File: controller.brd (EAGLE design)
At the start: 61 x 38.1 mm, 26 parts, among them U1 ATMEGA328P_PDIP, Y1 16MHz

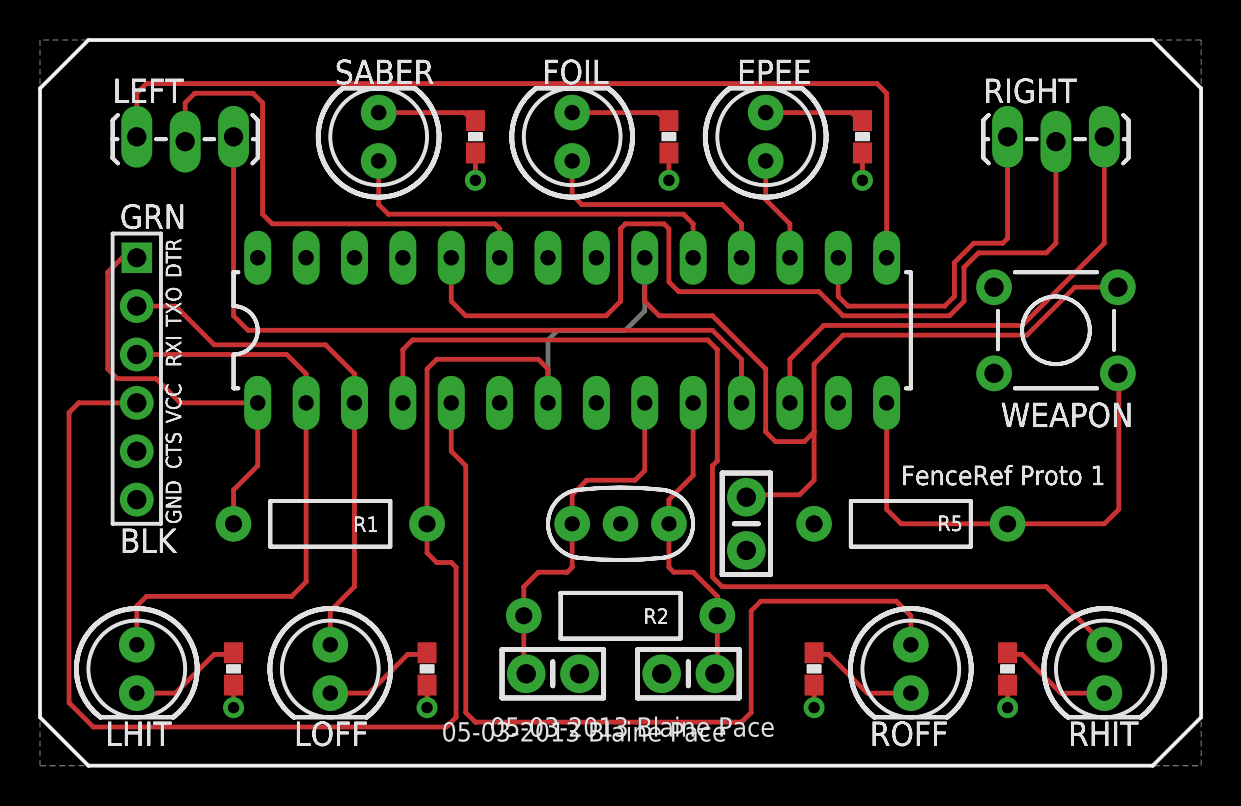
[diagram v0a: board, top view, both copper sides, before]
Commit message: Replaced resonator with crystal and updated CAM job
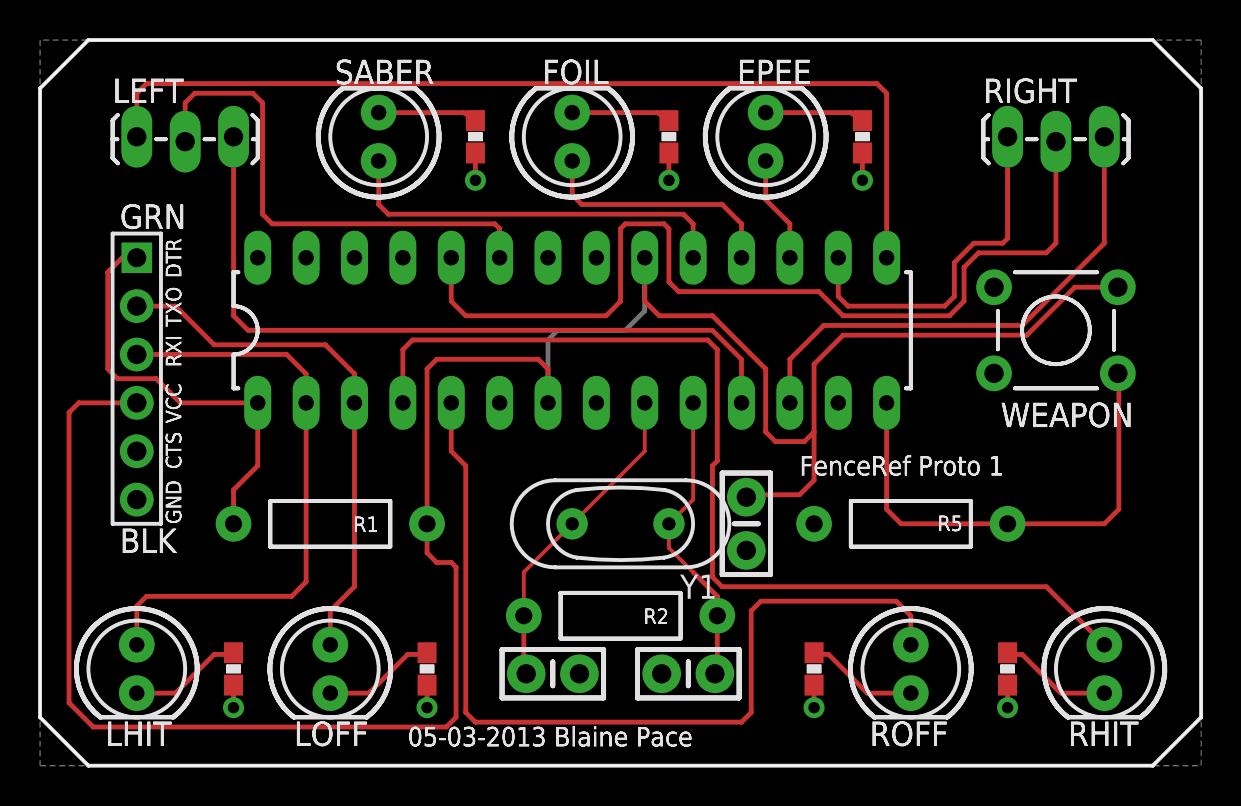
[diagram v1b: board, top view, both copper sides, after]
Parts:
- Y1: value 16MHz -> (none); device SparkFun-FreqCtrl:RESONATOR-PTH -> SparkFun-FreqCtrl:HC49US
- turned Y1 to 180 degrees
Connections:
- net GND: no longer Y1.2
- net XTAL1: now also Y1.2; no longer Y1.1
- net XTAL2: now also Y1.1; no longer Y1.3
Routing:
- net XTAL1: track 19.3 -> 16.9 mm
- net XTAL2: track 16.4 -> 15.9 mm
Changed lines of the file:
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@@
 <wire x1="2.54" y1="0" x2="0" y2="2.54" width="0" layer="20"/>
 <wire x1="0" y1="2.54" x2="0" y2="35.56" width="0" layer="20"/>
-<text x="45.212" y="14.732" size="1.016" layer="21">FenceRef Proto 1</text>
-<text x="23.622" y="1.524" size="1.016" layer="21">05-03-2013 Blaine Pace</text>
+<text x="39.878" y="15.24" size="1.016" layer="21">FenceRef Proto 1</text>
+<text x="19.304" y="1.016" size="1.016" layer="21">05-03-2013 Blaine Pace</text>
 <wire x1="37.719" y1="12.7" x2="36.449" y2="12.7" width="0.254" layer="121"/>
 <wire x1="38.354" y1="15.367" x2="38.354" y2="10.033" width="0.254" layer="121"/>
@@
 <wire x1="0" y1="2.54" x2="0" y2="35.56" width="0.2032" layer="121"/>
 <wire x1="0" y1="2.54" x2="0" y2="35.56" width="0.2032" layer="122"/>
-<text x="45.212" y="14.732" size="1.016" layer="121" font="vector" ratio="20">FenceRef Proto 1</text>
-<text x="21.082" y="1.27" size="1.016" layer="121" font="vector" ratio="20">05-03-2013 Blaine Pace</text>
+<text x="39.878" y="15.24" size="1.016" layer="121" font="vector" ratio="20">FenceRef Proto 1</text>
+<text x="19.304" y="1.016" size="1.016" layer="121" font="vector" ratio="20">05-03-2013 Blaine Pace</text>
 </plain>
 <attributes>
@@
 <attribute name="NAME" x="33.02" y="8.255" size="0.8128" layer="25" font="vector" ratio="15" rot="R180"/>
 </element>
-<element name="Y1" library="SparkFun-FreqCtrl" package="RESONATOR-PTH" value="16MHz" x="30.48" y="12.7"/>
 <element name="C2" library="SparkFun-Capacitors" package="CAP-PTH-SMALL-KIT" value="22pF" x="26.924" y="4.826"/>
 <element name="C3" library="SparkFun-Capacitors" package="CAP-PTH-SMALL-KIT" value="22pF" x="34.036" y="4.826" rot="R180"/>
@@
 <element name="LEFT" library="SparkFun-Connectors" package="1X03_LOCK_LONGPADS" value="" x="5.08" y="33.02"/>
 <element name="RIGHT" library="SparkFun-Connectors" package="1X03_LOCK_LONGPADS" value="" x="50.8" y="33.02"/>
+<element name="Y1" library="SparkFun-FreqCtrl" package="HC49US" value="" x="30.48" y="12.7" rot="R180"/>
 </elements>
 <signals>
@@
 <contactref element="C2" pad="2"/>
 <contactref element="C3" pad="2"/>
-<contactref element="Y1" pad="2"/>
 <contactref element="U1" pad="8"/>
 <contactref element="U1" pad="22"/>
@@
 <wire x1="31.75" y1="24.384" x2="31.75" y2="26.67" width="0.254" layer="1"/>
 </signal>
-<signal name="XTAL1">
-<contactref element="U1" pad="9"/>
-<contactref element="Y1" pad="1"/>
-<contactref element="C2" pad="1"/>
-<contactref element="R2" pad="P$2"/>
-<wire x1="31.75" y1="19.05" x2="31.75" y2="15.494" width="0.254" layer="1"/>
-<wire x1="31.75" y1="15.494" x2="31.242" y2="14.986" width="0.254" layer="1"/>
-<wire x1="31.242" y1="14.986" x2="28.702" y2="14.986" width="0.254" layer="1"/>
-<wire x1="28.702" y1="14.986" x2="27.94" y2="14.224" width="0.254" layer="1"/>
-<wire x1="27.94" y1="14.224" x2="27.94" y2="12.7" width="0.254" layer="1"/>
-<wire x1="27.94" y1="12.7" x2="27.94" y2="10.414" width="0.254" layer="1"/>
-<wire x1="27.94" y1="10.414" x2="27.686" y2="10.16" width="0.254" layer="1"/>
-<wire x1="27.686" y1="10.16" x2="26.162" y2="10.16" width="0.254" layer="1"/>
-<wire x1="26.162" y1="10.16" x2="25.4" y2="9.398" width="0.254" layer="1"/>
-<wire x1="25.4" y1="9.398" x2="25.4" y2="7.874" width="0.254" layer="1"/>
-<wire x1="25.4" y1="7.874" x2="25.4" y2="4.953" width="0.254" layer="1"/>
-<wire x1="25.4" y1="4.953" x2="25.527" y2="4.826" width="0.254" layer="1"/>
-</signal>
-<signal name="XTAL2">
-<contactref element="U1" pad="10"/>
-<contactref element="Y1" pad="3"/>
-<contactref element="R2" pad="P$1"/>
-<contactref element="C3" pad="1"/>
-<wire x1="35.56" y1="7.874" x2="35.56" y2="8.89" width="0.254" layer="1"/>
-<wire x1="35.56" y1="8.89" x2="34.29" y2="10.16" width="0.254" layer="1"/>
-<wire x1="34.29" y1="10.16" x2="33.274" y2="10.16" width="0.254" layer="1"/>
-<wire x1="33.274" y1="10.16" x2="33.02" y2="10.414" width="0.254" layer="1"/>
-<wire x1="33.02" y1="10.414" x2="33.02" y2="12.7" width="0.254" layer="1"/>
-<wire x1="33.02" y1="12.7" x2="33.02" y2="13.97" width="0.254" layer="1"/>
-<wire x1="33.02" y1="13.97" x2="34.29" y2="15.24" width="0.254" layer="1"/>
-<wire x1="34.29" y1="15.24" x2="34.29" y2="19.05" width="0.254" layer="1"/>
-<wire x1="35.56" y1="7.874" x2="35.56" y2="4.953" width="0.254" layer="1"/>
-<wire x1="35.56" y1="4.953" x2="35.433" y2="4.826" width="0.254" layer="1"/>
-</signal>
 <signal name="L_GND">
 <contactref element="U1" pad="11"/>
@@
 <wire x1="22.24" y1="34.29" x2="17.78" y2="34.29" width="0.254" layer="1"/>
 </signal>
+<signal name="XTAL1">
+<contactref element="Y1" pad="2"/>
+<contactref element="U1" pad="9"/>
+<contactref element="C2" pad="1"/>
+<contactref element="R2" pad="P$2"/>
+<wire x1="25.4" y1="7.874" x2="25.4" y2="4.953" width="0.254" layer="1"/>
+<wire x1="25.4" y1="4.953" x2="25.527" y2="4.826" width="0.254" layer="1"/>
+<wire x1="25.4" y1="7.874" x2="25.4" y2="10.16" width="0.2032" layer="1"/>
+<wire x1="25.4" y1="10.16" x2="27.94" y2="12.7" width="0.2032" layer="1"/>
+<wire x1="27.94" y1="12.7" x2="31.75" y2="16.51" width="0.2032" layer="1"/>
+<wire x1="31.75" y1="16.51" x2="31.75" y2="19.05" width="0.2032" layer="1"/>
+</signal>
+<signal name="XTAL2">
+<contactref element="U1" pad="10"/>
+<contactref element="Y1" pad="1"/>
+<contactref element="R2" pad="P$1"/>
+<contactref element="C3" pad="1"/>
+<wire x1="35.56" y1="7.874" x2="35.56" y2="8.89" width="0.254" layer="1"/>
+<wire x1="35.56" y1="8.89" x2="34.29" y2="10.16" width="0.254" layer="1"/>
+<wire x1="35.56" y1="7.874" x2="35.56" y2="4.953" width="0.254" layer="1"/>
+<wire x1="35.56" y1="4.953" x2="35.433" y2="4.826" width="0.254" layer="1"/>
+<wire x1="34.29" y1="10.16" x2="33.02" y2="11.43" width="0.2032" layer="1"/>
+<wire x1="33.02" y1="11.43" x2="33.02" y2="12.7" width="0.2032" layer="1"/>
+<wire x1="33.02" y1="12.7" x2="34.29" y2="13.97" width="0.2032" layer="1"/>
+<wire x1="34.29" y1="13.97" x2="34.29" y2="19.05" width="0.2032" layer="1"/>
+</signal>
 </signals>

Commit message: Finalized CAM setup
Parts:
- moved Y1 2.54 mm to (27.9, 12.7)
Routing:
- net XTAL2: track 15.9 -> 21.1 mm
- net XTAL1: track 16.9 -> 20.2 mm
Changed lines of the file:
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@@
 <layer number="19" name="Unrouted" color="6" fill="1" visible="yes" active="yes"/>
 <layer number="20" name="Dimension" color="15" fill="1" visible="no" active="yes"/>
-<layer number="21" name="tPlace" color="7" fill="1" visible="no" active="yes"/>
+<layer number="21" name="tPlace" color="7" fill="1" visible="yes" active="yes"/>
 <layer number="22" name="bPlace" color="7" fill="1" visible="no" active="yes"/>
 <layer number="23" name="tOrigins" color="15" fill="1" visible="yes" active="yes"/>
@@
 <layer number="107" name="Crop" color="7" fill="1" visible="no" active="yes"/>
 <layer number="116" name="Patch_BOT" color="9" fill="4" visible="no" active="yes"/>
-<layer number="121" name="_tsilk" color="14" fill="1" visible="yes" active="yes"/>
-<layer number="122" name="_bsilk" color="14" fill="1" visible="yes" active="yes"/>
+<layer number="121" name="_tsilk" color="14" fill="1" visible="no" active="yes"/>
+<layer number="122" name="_bsilk" color="14" fill="1" visible="no" active="yes"/>
 <layer number="125" name="_tNames" color="7" fill="1" visible="no" active="yes"/>
 <layer number="144" name="Drill_legend" color="7" fill="1" visible="no" active="yes"/>
@@
 <element name="LEFT" library="SparkFun-Connectors" package="1X03_LOCK_LONGPADS" value="" x="5.08" y="33.02"/>
 <element name="RIGHT" library="SparkFun-Connectors" package="1X03_LOCK_LONGPADS" value="" x="50.8" y="33.02"/>
-<element name="Y1" library="SparkFun-FreqCtrl" package="HC49US" value="" x="30.48" y="12.7" rot="R180"/>
+<element name="Y1" library="SparkFun-FreqCtrl" package="HC49US" value="" x="27.94" y="12.7" rot="R180"/>
 </elements>
 <signals>
@@
 <wire x1="25.4" y1="7.874" x2="25.4" y2="4.953" width="0.254" layer="1"/>
 <wire x1="25.4" y1="4.953" x2="25.527" y2="4.826" width="0.254" layer="1"/>
-<wire x1="25.4" y1="7.874" x2="25.4" y2="10.16" width="0.2032" layer="1"/>
-<wire x1="25.4" y1="10.16" x2="27.94" y2="12.7" width="0.2032" layer="1"/>
-<wire x1="27.94" y1="12.7" x2="31.75" y2="16.51" width="0.2032" layer="1"/>
-<wire x1="31.75" y1="16.51" x2="31.75" y2="19.05" width="0.2032" layer="1"/>
+<wire x1="25.4" y1="7.874" x2="25.4" y2="12.7" width="0.2032" layer="1"/>
+<wire x1="31.75" y1="19.05" x2="31.75" y2="15.494" width="0.2032" layer="1"/>
+<wire x1="31.75" y1="15.494" x2="31.496" y2="15.24" width="0.2032" layer="1"/>
+<wire x1="31.496" y1="15.24" x2="25.908" y2="15.24" width="0.2032" layer="1"/>
+<wire x1="25.908" y1="15.24" x2="25.4" y2="14.732" width="0.2032" layer="1"/>
+<wire x1="25.4" y1="14.732" x2="25.4" y2="12.7" width="0.2032" layer="1"/>
 </signal>
 <signal name="XTAL2">
@@
 <contactref element="R2" pad="P$1"/>
 <contactref element="C3" pad="1"/>
-<wire x1="35.56" y1="7.874" x2="35.56" y2="8.89" width="0.254" layer="1"/>
-<wire x1="35.56" y1="8.89" x2="34.29" y2="10.16" width="0.254" layer="1"/>
 <wire x1="35.56" y1="7.874" x2="35.56" y2="4.953" width="0.254" layer="1"/>
 <wire x1="35.56" y1="4.953" x2="35.433" y2="4.826" width="0.254" layer="1"/>
-<wire x1="34.29" y1="10.16" x2="33.02" y2="11.43" width="0.2032" layer="1"/>
-<wire x1="33.02" y1="11.43" x2="33.02" y2="12.7" width="0.2032" layer="1"/>
-<wire x1="33.02" y1="12.7" x2="34.29" y2="13.97" width="0.2032" layer="1"/>
-<wire x1="34.29" y1="13.97" x2="34.29" y2="19.05" width="0.2032" layer="1"/>
+<wire x1="35.56" y1="7.874" x2="33.528" y2="9.906" width="0.2032" layer="1"/>
+<wire x1="33.528" y1="9.906" x2="30.988" y2="9.906" width="0.2032" layer="1"/>
+<wire x1="30.988" y1="9.906" x2="30.48" y2="10.414" width="0.2032" layer="1"/>
+<wire x1="30.48" y1="10.414" x2="30.48" y2="12.7" width="0.2032" layer="1"/>
+<wire x1="30.48" y1="12.7" x2="30.48" y2="14.224" width="0.2032" layer="1"/>
+<wire x1="30.48" y1="14.224" x2="30.988" y2="14.732" width="0.2032" layer="1"/>
+<wire x1="30.988" y1="14.732" x2="33.782" y2="14.732" width="0.2032" layer="1"/>
+<wire x1="33.782" y1="14.732" x2="34.29" y2="15.24" width="0.2032" layer="1"/>
+<wire x1="34.29" y1="15.24" x2="34.29" y2="19.05" width="0.2032" layer="1"/>
 </signal>
 </signals>
